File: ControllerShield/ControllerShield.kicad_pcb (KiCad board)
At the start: 2 copper layers, 68.6 x 53.5 mm, 24 parts, among them J1 Power, J2 Digital/PWM, J3 Analog, J4 Digital/PWM, J5 Conn_02x05_Odd_Even, J6 Debug Point, SW1 Small Switch TH, U1 COM-09032, U2 LIS3DHTR, U3 TLV75533PDBV

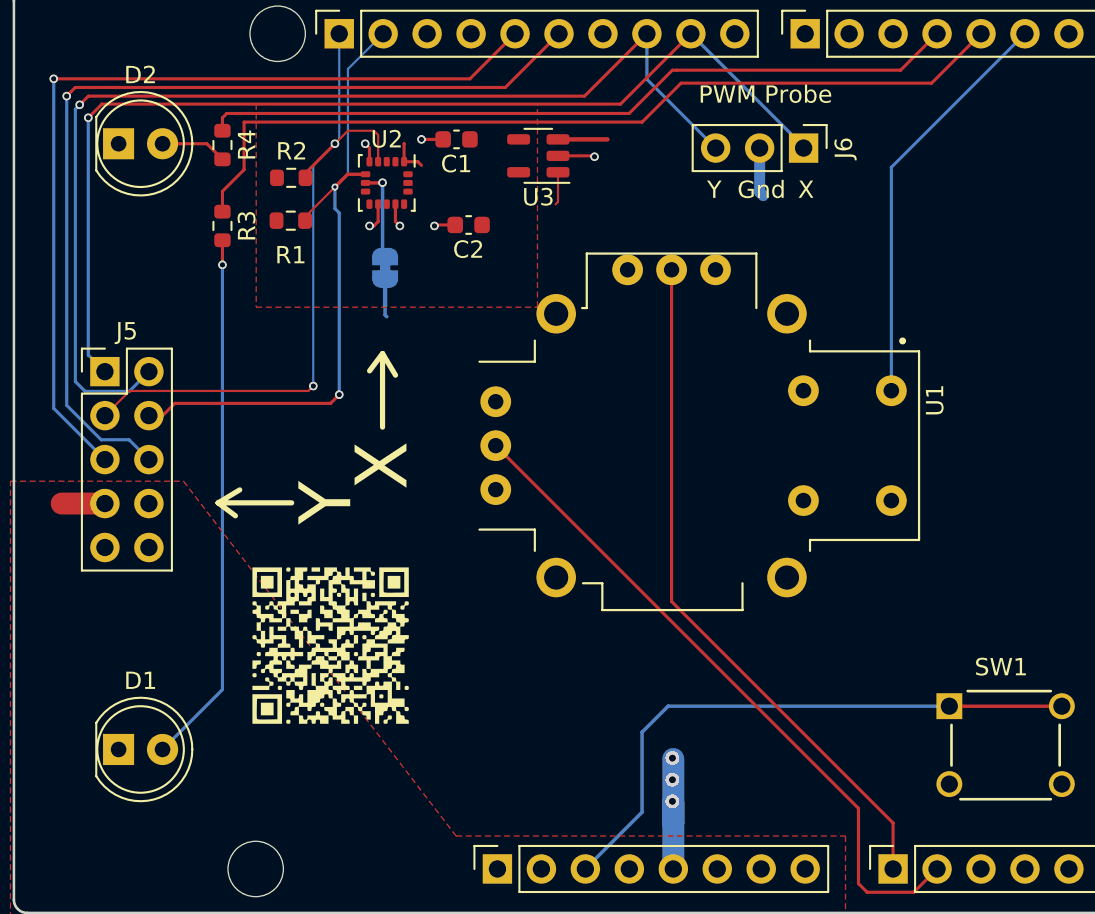
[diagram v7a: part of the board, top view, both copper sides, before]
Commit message: Change footprint for level shifter to something more reasonable.
Add lots of cap to controller.

Add level shifter to controller
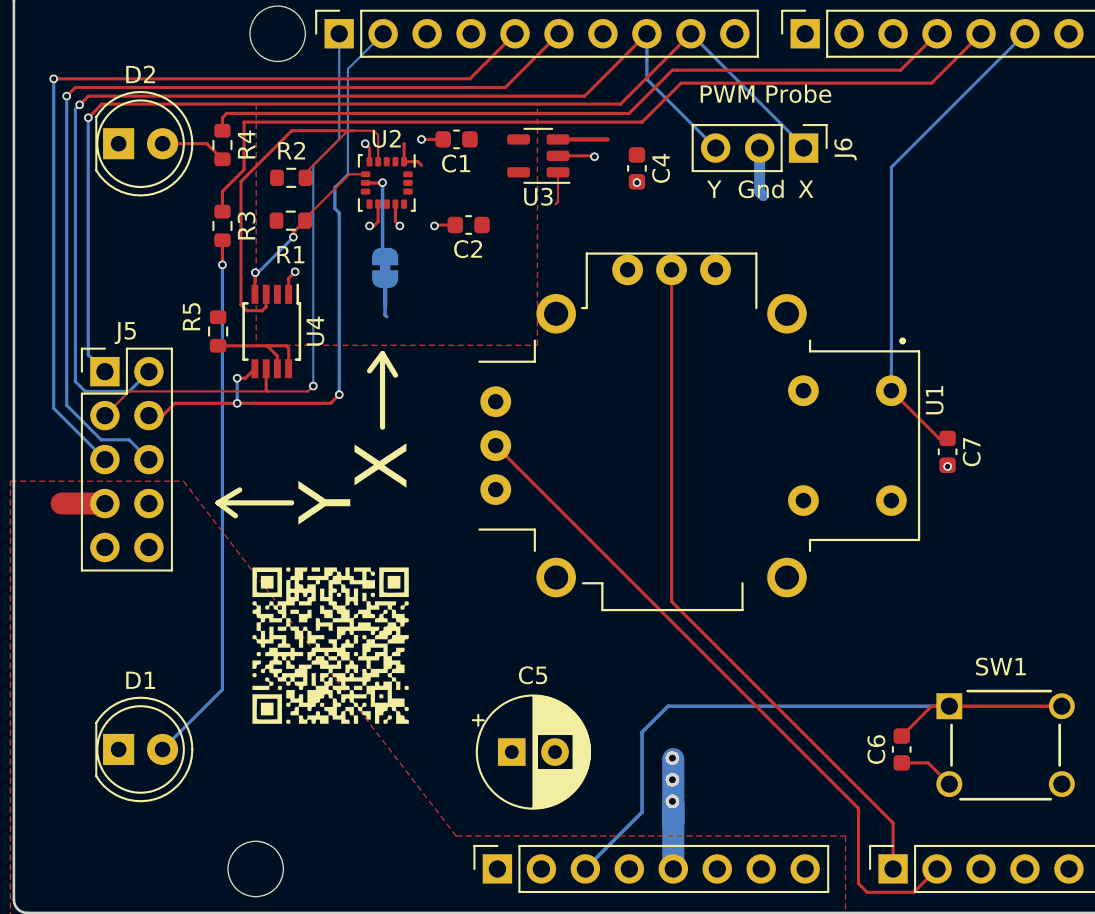
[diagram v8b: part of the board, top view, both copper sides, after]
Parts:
- added C4: 1uF, Capacitor_SMD:C_0603_1608Metric, F.Cu at (157.9, 98.2)
- added C5: 10uF, Capacitor_THT:CP_Radial_D6.3mm_P2.50mm, F.Cu at (150.7, 131.9)
- added C6: 0.1uF, Capacitor_SMD:C_0603_1608Metric, F.Cu at (173.2, 131.8)
- added C7: 0.1uF, Capacitor_SMD:C_0603_1608Metric, F.Cu at (175.9, 114.5)
- added R5: 200K, Resistor_SMD:R_0603_1608Metric, F.Cu at (133.8, 107.6)
- added U4: PCA9306DQER, Package_SO:TSSOP-8_3x3mm_P0.65mm, F.Cu at (136.8, 107.6)
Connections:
- R1 pad 2: /SDA -> /SDA3p3
- R2 pad 2: /SCL -> /SCL3p3
- U2 pad 4: /SCL -> /SCL3p3
- U2 pad 6: /SDA -> /SDA3p3
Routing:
- net /SCL3p3: track 0.00 -> 24.4 mm
- net /SDA3p3: track 0.00 -> 10.1 mm, vias 0 -> 2
- net Net-(U4-EN): track 0.00 -> 6.88 mm
- net /SCL: track 40.8 -> 35.1 mm, vias 2 -> 1
- net GND: track 15.4 -> 20.1 mm, vias 6 -> 9
- net /GameBtn: track 23.8 -> 28.2 mm
- net /RSTn: track 34.1 -> 37.6 mm
- net /SDA: track 38.3 -> 36.3 mm, vias 2 -> 3
